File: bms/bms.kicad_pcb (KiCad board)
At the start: 2 copper layers, 134 x 125 mm, 27 parts, among them J10 Conn_02x08_Odd_Even, J11 Conn_02x10_Odd_Even, J13 Conn_02x08_Odd_Even, J14 Conn_02x08_Odd_Even, J2 Conn_01x08_Socket, J22 Conn_02x10_Odd_Even, J3 Conn_01x06_Socket, J5 Conn_01x10_Socket, J6 Conn_01x06_Socket

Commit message: v0.99
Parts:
- added CAN_Bus_VCU1: Conn_01x02_Pin, Connector_PinHeader_2.00mm:PinHeader_1x02_P2.00mm_Vertical, F.Cu at (93.3, 39.8)
- added CAN_k312: Conn_01x02_Pin, Connector_PinHeader_2.54mm:PinHeader_1x02_P2.54mm_Vertical, F.Cu at (93.1, 43.5)
- added D1: SS32, Diode_SMD:D_SMB, F.Cu at (68.2, 45.4)
- J6: value Conn_01x06_Socket -> Conn_01x08_Socket; footprint Connector_PinSocket_2.54mm:PinSocket_1x06_P2.54mm_Vertical -> Connector_PinSocket_2.54mm:PinSocket_1x08_P2.54mm_Vertical
- moved Battery1 150.4 mm to (63.3, 46.2), turned to 90 degrees
- moved Vdd1 131.1 mm to (117.0, 77.0), turned to -90 degrees
- moved J11 104.0 mm to (125.0, 128.6)
- moved J10 104.0 mm to (125.0, 100.7)
- moved J13 104.0 mm to (76.8, 65.1)
- moved J14 104.0 mm to (76.8, 88.0)
- moved J22 104.0 mm to (76.8, 110.9)
- moved J2 94.4 mm to (97.6, 104.9)
- moved J3 94.4 mm to (97.6, 127.7)
- moved J5 94.2 mm to (145.8, 96.1)
- moved J6 94.2 mm to (145.8, 122.7)
- moved Soft_G_B5-6 93.5 mm to (63.2, 73.2), turned to 90 degrees
- moved Soft_G_B7-8 92.9 mm to (63.2, 82.2), turned to 90 degrees
- moved Soft_G_B13-14 90.0 mm to (63.2, 109.2), turned to 90 degrees
- moved Soft_G_B15-16 89.8 mm to (63.2, 118.2), turned to 90 degrees
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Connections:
- J13 pad 1: unconnected-(J13-Pin_1-Pad1) -> Bat+
- J13 pad 10: unconnected-(J13-Pin_10-Pad10) -> G5
- J13 pad 12: unconnected-(J13-Pin_12-Pad12) -> G6
- J13 pad 13: unconnected-(J13-Pin_13-Pad13) -> GND
- J13 pad 14: unconnected-(J13-Pin_14-Pad14) -> G7
- J13 pad 16: unconnected-(J13-Pin_16-Pad16) -> G8
- J13 pad 2: unconnected-(J13-Pin_2-Pad2) -> G1
- J13 pad 4: unconnected-(J13-Pin_4-Pad4) -> G2
- J13 pad 6: unconnected-(J13-Pin_6-Pad6) -> G3
- J13 pad 8: unconnected-(J13-Pin_8-Pad8) -> G4
- J13 pad 9: unconnected-(J13-Pin_9-Pad9) -> Vdd
- J14 pad 1: unconnected-(J14-Pin_1-Pad1) -> 1
- J14 pad 10: unconnected-(J14-Pin_10-Pad10) -> G13
- J14 pad 11: unconnected-(J14-Pin_11-Pad11) -> 6
- J14 pad 12: unconnected-(J14-Pin_12-Pad12) -> G14
- J14 pad 13: unconnected-(J14-Pin_13-Pad13) -> 7
- J14 pad 14: unconnected-(J14-Pin_14-Pad14) -> G15
- J14 pad 15: unconnected-(J14-Pin_15-Pad15) -> 8
- J14 pad 16: unconnected-(J14-Pin_16-Pad16) -> G16
- J14 pad 2: unconnected-(J14-Pin_2-Pad2) -> G9
- J14 pad 3: unconnected-(J14-Pin_3-Pad3) -> 2
- J14 pad 4: unconnected-(J14-Pin_4-Pad4) -> G10
- J14 pad 5: unconnected-(J14-Pin_5-Pad5) -> 3
- J14 pad 6: unconnected-(J14-Pin_6-Pad6) -> G11
- J14 pad 7: unconnected-(J14-Pin_7-Pad7) -> 4
- J14 pad 8: unconnected-(J14-Pin_8-Pad8) -> G12
- J14 pad 9: unconnected-(J14-Pin_9-Pad9) -> 5
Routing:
- net Vdd: track 0.00 -> 96.7 mm
- net 3: track 58.5 -> 105.9 mm
- net 5: track 58.5 -> 105.5 mm
- net 4: track 58.5 -> 105.5 mm
- net 2: track 58.5 -> 105.5 mm
- net 1: track 58.5 -> 105.2 mm
- net 6: track 58.5 -> 104.5 mm
- net 7: track 58.5 -> 103.9 mm
- net 8: track 58.5 -> 102.6 mm
- net Bat+: track 0.00 -> 30.5 mm
- net G15: track 0.00 -> 17.0 mm
- net G16: track 0.00 -> 17.0 mm
- net G2: track 0.00 -> 17.0 mm
- net G1: track 0.00 -> 16.9 mm
- net G13: track 0.00 -> 14.5 mm
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- added copper zone on B.Cu, net GND
- added copper zone on F.Cu, net GND
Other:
- board size 134 x 125 mm -> 100 x 108.1 mm

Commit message: V0.999 a little more polished
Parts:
- added J10: Conn_02x10_Odd_Even, Connector_PinHeader_2.54mm:PinHeader_2x10_P2.54mm_Vertical, B.Cu at (118.0, 103.4)
- CAN_k312: moved to B.Cu
- moved Conn_Thermistors_2 59.7 mm to (94.7, 32.9), turned to 0 degrees
- moved Conn_Thermistors_3 49.3 mm to (94.7, 41.2), turned to 0 degrees
- moved Conn_Thermistors_4 39.8 mm to (94.7, 49.5), turned to 0 degrees
- moved Conn_Thermistors_1 38.9 mm to (94.7, 91.3), turned to 0 degrees
- moved Conn_Thermistors_5 31.8 mm to (94.7, 57.9), turned to 0 degrees
- moved Conn_Thermistors_8 31.1 mm to (94.7, 83.0), turned to 0 degrees
- moved J3 28.5 mm to (83.5, 152.4)
- moved J5 28.5 mm to (131.7, 120.8)
- moved J6 28.5 mm to (131.7, 147.4)
- moved J2 28.5 mm to (83.5, 129.6)
- moved Conn_Thermistors_6 26.8 mm to (94.7, 66.2), turned to 0 degrees
- moved Conn_Thermistors_7 26.5 mm to (94.7, 74.6), turned to 0 degrees
- moved J11 25.5 mm to (118.0, 125.2)
- moved J12 25.5 mm to (118.0, 153.2)
- moved J13 25.5 mm to (69.8, 89.7)
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- renumbered J10 to J11, J11 to J12, J22 to J15
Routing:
- net SCK: track 0.00 -> 40.6 mm
- net MISO: track 0.00 -> 40.2 mm
- net SOUT: track 0.00 -> 39.8 mm
- net CS: track 0.00 -> 39.4 mm
- net CAN_L_k: track 4.56 -> 40.1 mm
- net CAN_H_k: track 4.54 -> 39.9 mm
- net Bat+: track 30.5 -> 63.2 mm
- net 8: track 102.6 -> 117.1 mm
- net 1: track 105.2 -> 92.2 mm
- net 2: track 105.5 -> 95.8 mm
- net 7: track 103.9 -> 113.5 mm
- net 3: track 105.9 -> 99.3 mm
- net Vdd: track 96.7 -> 90.5 mm
- net 6: track 104.5 -> 110.1 mm
- net G5: track 13.0 -> 10.4 mm
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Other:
- board size 100 x 108.1 mm -> 85.7 x 143.9 mm

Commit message: inca un update
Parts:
- CAN_Bus_VCU1: footprint Connector_PinHeader_2.00mm:PinHeader_1x02_P2.00mm_Vertical -> Connector_JST:JST_PH_S2B-PH-K_1x02_P2.00mm_Horizontal
- moved CAN_Bus_VCU1 3.99 mm to (88.2, 32.3), turned to 180 degrees
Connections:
- CAN_Bus_VCU1 pad 1: CAN_L_k -> CAN_H_k
- CAN_Bus_VCU1 pad 2: CAN_H_k -> CAN_L_k
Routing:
- net CAN_L_k: track 40.1 -> 36.6 mm
- net CAN_H_k: track 39.9 -> 36.5 mm

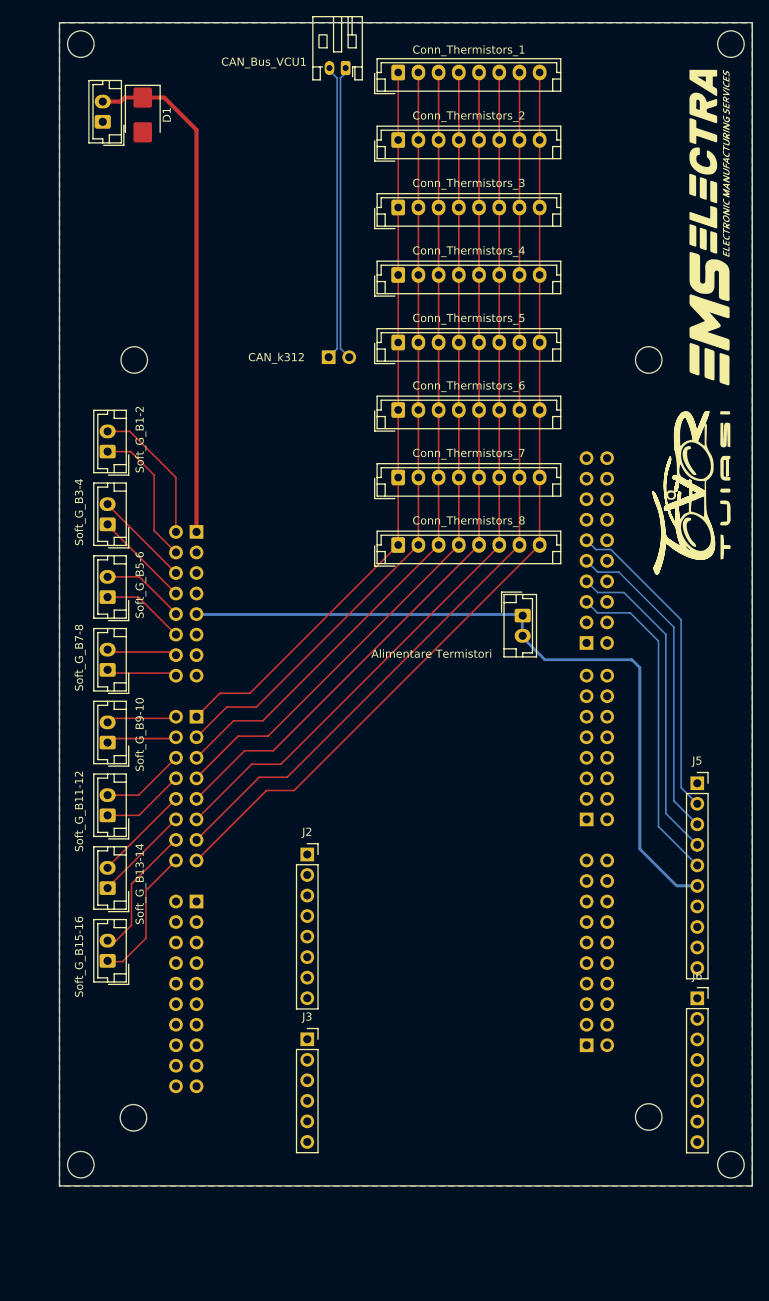
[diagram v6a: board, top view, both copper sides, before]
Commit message: Check on layout+block diagram
4x mounting holes with GND connection - added;
PCB size small increaze
block diagram reshaped
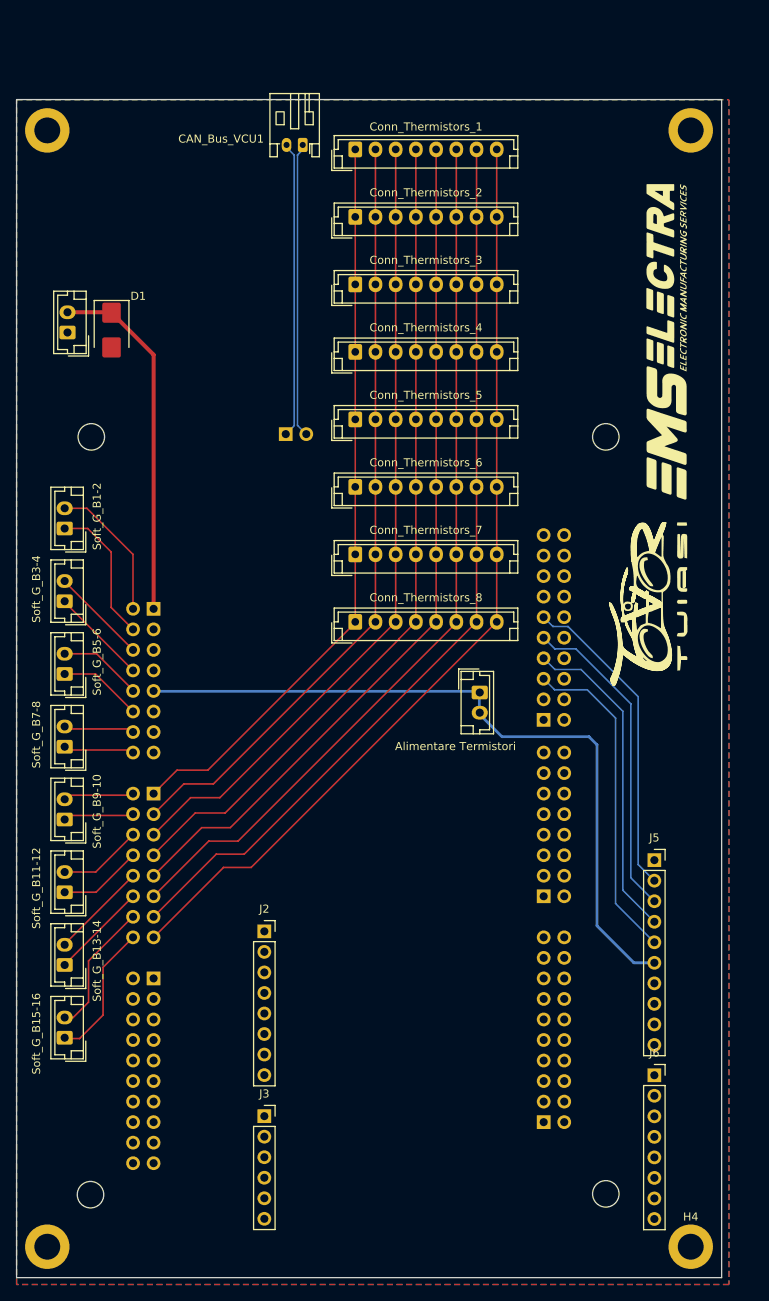
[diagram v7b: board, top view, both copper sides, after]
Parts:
- added H1: MountingHole_Pad, MountingHole:MountingHole_3.2mm_M3_ISO14580_Pad, F.Cu at (130.9, 40.0)
- added H2: MountingHole_Pad, MountingHole:MountingHole_3.2mm_M3_ISO14580_Pad, F.Cu at (51.3, 178.1)
- added H3: MountingHole_Pad, MountingHole:MountingHole_3.2mm_M3_ISO14580_Pad, F.Cu at (51.3, 40.0)
- added H4: MountingHole_Pad, MountingHole:MountingHole_3.2mm_M3_ISO14580_Pad, F.Cu at (130.9, 178.1)
- moved D1 26.9 mm to (59.2, 64.7)
- moved Battery1 26.4 mm to (53.8, 65.0)
- moved Conn_Thermistors_1 10.9 mm to (89.4, 100.8)
- moved Conn_Thermistors_7 10.9 mm to (89.4, 84.1)
- moved J12 10.9 mm to (112.7, 162.7)
- moved J15 10.9 mm to (64.4, 144.9)
- moved J2 10.9 mm to (78.1, 139.1)
- moved Soft_G_B13-14 10.9 mm to (53.4, 143.3)
- moved Soft_G_B15-16 10.9 mm to (53.4, 152.3)
- moved CAN_Bus_VCU1 10.9 mm to (82.9, 41.8)
- moved CAN_k312 10.9 mm to (80.8, 77.6)
- moved Conn_Thermistors_4 10.9 mm to (89.4, 59.1)
- moved Conn_Thermistors_5 10.9 mm to (89.4, 67.4)
- moved Conn_Thermistors_2 10.9 mm to (89.4, 42.4)
- moved Conn_Thermistors_3 10.9 mm to (89.4, 50.7)
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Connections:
- net Bat+ renamed BAT+
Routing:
- net BAT+: track 63.2 -> 44.3 mm
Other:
- board size 85.7 x 143.9 mm -> 87.2 x 145.7 mm

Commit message: added datasheets and revised layout to be continued
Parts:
- moved Soft_G_B1-2 90.8 mm to (102.0, 166.0), turned to 0 degrees
- moved Soft_G_B3-4 78.4 mm to (93.0, 166.0), turned to 0 degrees
- moved Soft_G_B5-6 66.2 mm to (84.0, 166.0), turned to 0 degrees
- moved Soft_G_B7-8 54.2 mm to (75.0, 166.0), turned to 0 degrees
- moved Soft_G_B9-10 53.2 mm to (101.5, 148.0), turned to 0 degrees
- moved Vdd1 48.6 mm to (59.0, 93.2), turned to 90 degrees
- moved Soft_G_B11-12 41.4 mm to (92.5, 148.0), turned to 0 degrees
- moved J2 40.0 mm to (55.8, 105.9)
- moved J5 40.0 mm to (104.0, 97.1)
- moved J6 40.0 mm to (104.0, 123.7)
- moved J3 40.0 mm to (55.8, 128.8)
- moved Soft_G_B13-14 30.4 mm to (83.5, 148.0), turned to 0 degrees
- moved Soft_G_B15-16 21.5 mm to (74.5, 148.0), turned to 0 degrees
- moved Conn_Thermistors_1 13.3 mm to (89.0, 87.5)
- moved Conn_Thermistors_3 13.3 mm to (89.0, 37.4)
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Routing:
- net SCK: track 40.6 -> 8.91 mm
- net MISO: track 40.2 -> 8.91 mm
- net SOUT: track 39.8 -> 8.91 mm
- net CS: track 39.4 -> 8.91 mm
- net G2: track 17.7 -> 0.00 mm
- net G1: track 17.6 -> 0.01 mm
- net G16: track 17.1 -> 0.00 mm
- net Vdd: track 90.5 -> 107.1 mm
- net G15: track 16.6 -> 0.05 mm
- net G4: track 12.1 -> 0.00 mm
- net G13: track 12.0 -> 0.00 mm
- net G3: track 12.0 -> 0.00 mm
- net G14: track 12.0 -> 0.00 mm
- net 8: track 117.1 -> 128.2 mm
- net 7: track 113.5 -> 124.6 mm
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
